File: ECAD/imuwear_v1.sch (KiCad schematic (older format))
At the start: 9 parts

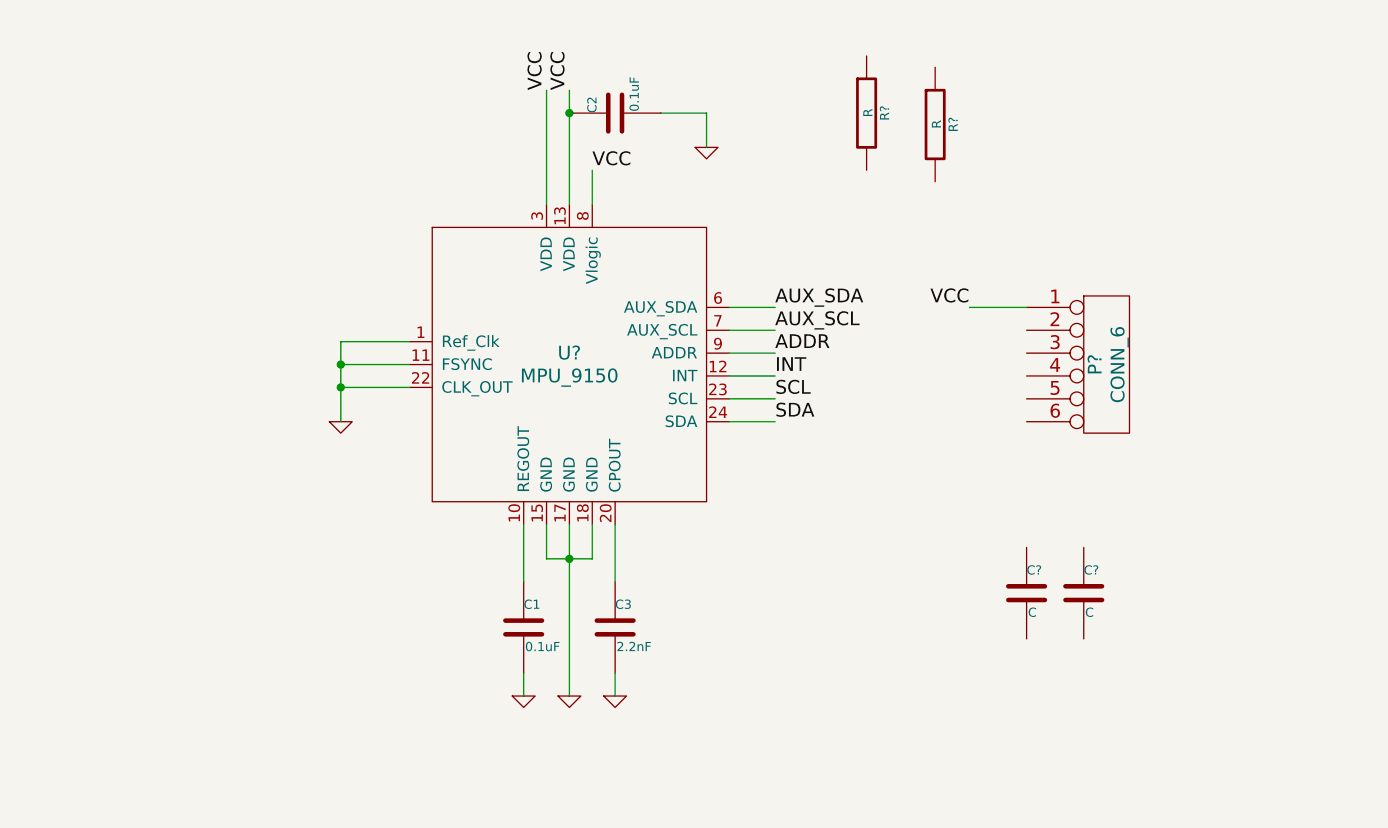
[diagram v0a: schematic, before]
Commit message: Added initial Netlist, Board, and Footprint Modules
Added footprints for 6 pin SMD and smallest throughole possible.
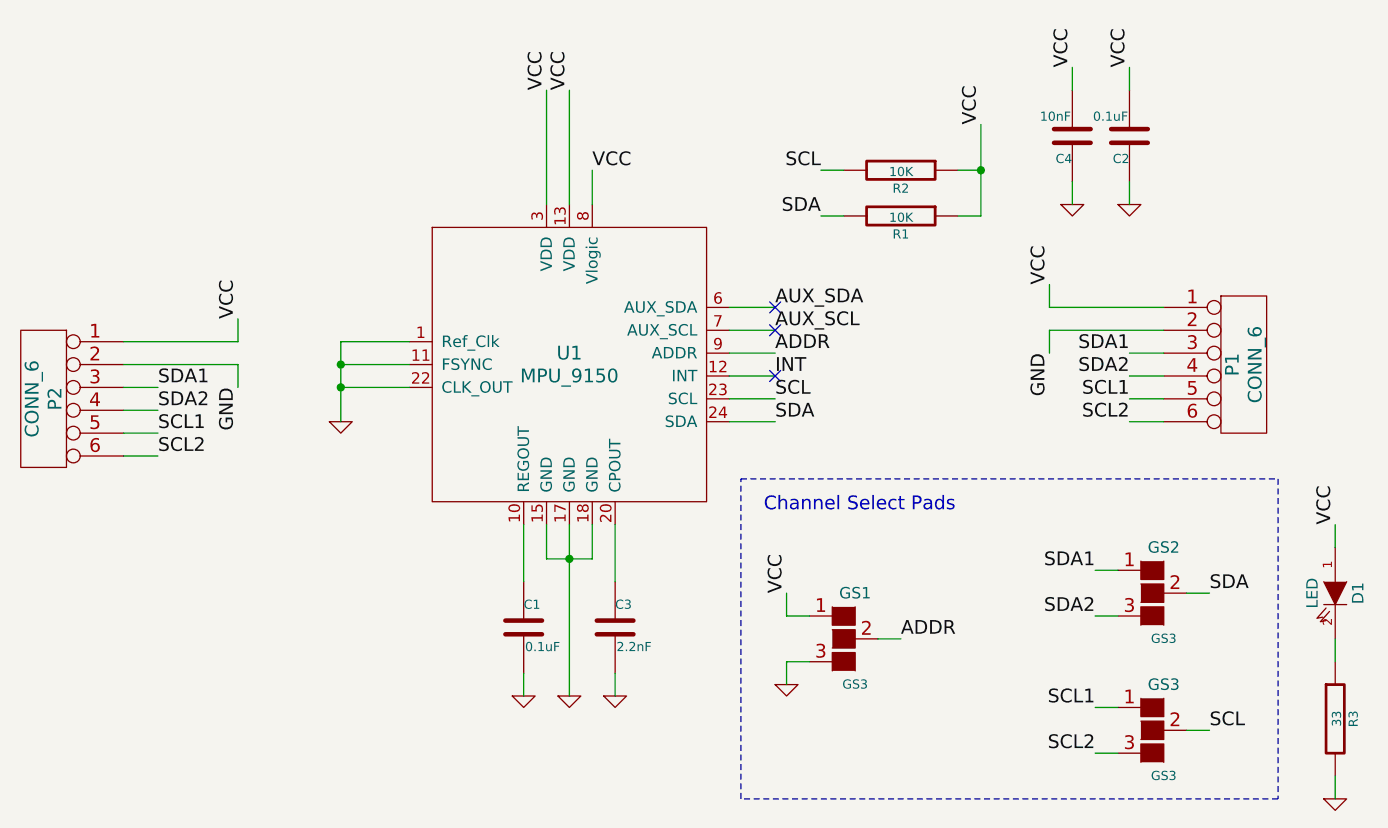
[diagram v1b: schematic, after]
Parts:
- removed C? (x2): C, ~, symbol C
- added C4: 10nF, ~, symbol C
- added D1: LED, ~, symbol LED
- added GS1, GS2, GS3: GS3, symbol GS3
- added P2: CONN_6, symbol CONN_6
- added R3: 33, ~, symbol R
- R1, R2: renamed from R?; value R -> 10K
- gave numbers to parts that had none: 2
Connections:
- net ADDR: now also GS1.2 (G2)
- net GND: now also C2.1, P1.2, C4.1, GS1.3 (G3), P2.2, R3.2; no longer C2.2
- net SCL: now also R2.2, GS3.2 (G2)
- net SDA: now also R1.2, GS2.2 (G2)
- net VCC: now also C2.2, R1.1, R2.1, C4.2, D1.1 (A), GS1.1 (G1), P2.1; no longer C2.1
- net SDA1: now reaches P1.3
- net SDA1: now also GS2.1 (G1), P2.3
- net SDA2: now reaches P1.4
- net SDA2: now also GS2.3 (G3), P2.4
- net SCL1: now reaches P1.5
- net SCL1: now also GS3.1 (G1), P2.5
- net SCL2: now reaches P1.6
- net SCL2: now also GS3.3 (G3), P2.6
- new net: D1.2 (K), R3.1
- no-connect marks 0 -> 3
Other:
- note added: "Channel Select Pads"
- moved on the sheet: C2, P1, R1, R2
